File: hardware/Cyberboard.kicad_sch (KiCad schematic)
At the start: 67 parts, among them J1 Conn_01x20, J2 Conn_01x20, SW1 SW_Push, SW2 SW_Push, U1 TPS630701RNMR, U2 NX2012SA-32.768KHZ-STD-MUB-2, U3 XL-1005UBC_C22355736, U4 STM32WB55RGVx, U5 BQ24074RGT, U6 TPD2EUSB30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

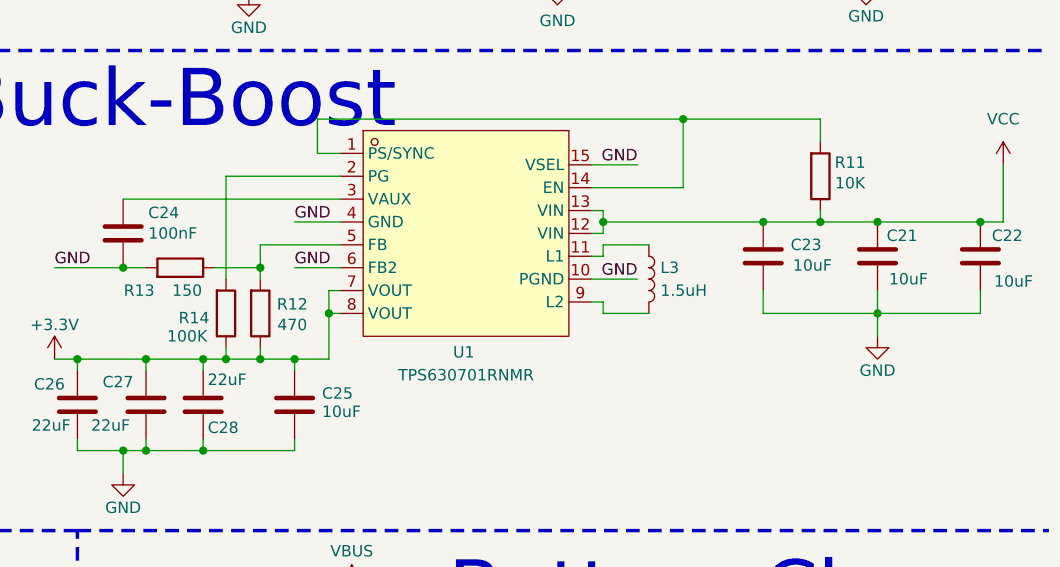
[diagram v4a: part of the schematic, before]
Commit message: forgot resistor values and change in inductor footprint
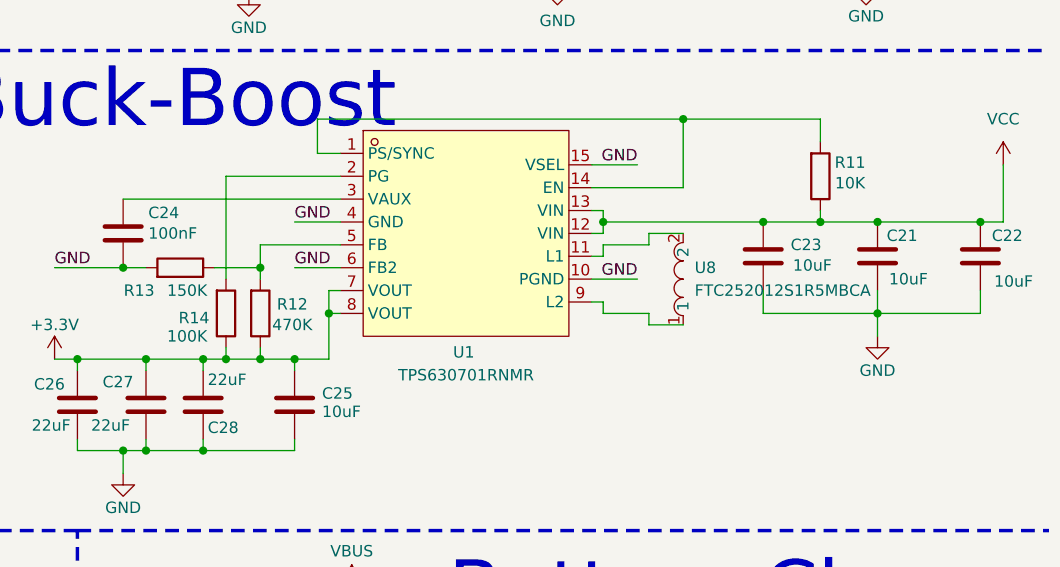
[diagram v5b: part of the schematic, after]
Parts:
- removed L3: 1.5uH, Inductor_SMD:L_0603_1608Metric, symbol Device:L
- added U8: FTC252012S1R5MBCA, lcsc:IND-SMD_L2.5-W2.0_MEKK2520TR47M, symbol lcsc:FTC252012S1R5MBCA
- R12: value 470 -> 470K
- R13: value 150 -> 150K
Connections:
- net at U1.11 (L1): now also U8.2
- net at U1.9 (L2): now also U8.1
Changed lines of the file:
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@@
 	(wire
 		(pts
+			(xy 240.03 78.74) (xy 243.84 78.74)
+		)
+		(stroke
+			(width 0)
+			(type default)
+		)
+	)
+	(wire
+		(pts
 			(xy 86.36 55.88) (xy 100.33 55.88)
 		)
@@
 	(wire
 		(pts
+			(xy 240.03 88.9) (xy 243.84 88.9)
+		)
+		(stroke
+			(width 0)
+			(type default)
+		)
+	)
+	(wire
+		(pts
 			(xy 106.68 168.91) (xy 119.38 168.91)
 		)
@@
 	(wire
 		(pts
+			(xy 240.03 87.63) (xy 240.03 88.9)
+		)
+		(stroke
+			(width 0)
+			(type default)
+		)
+	)
+	(wire
+		(pts
 			(xy 271.78 21.59) (xy 259.08 21.59)
 		)
@@
 	(wire
 		(pts
+			(xy 240.03 80.01) (xy 240.03 78.74)
+		)
+		(stroke
+			(width 0)
+			(type default)
+		)
+	)
+	(wire
+		(pts
 			(xy 265.43 77.47) (xy 276.86 77.47)
 		)
@@
 			)
 		)
-		(property "Value" "150"
+		(property "Value" "150K"
 			(at 188.722 85.09 90)
 			(effects
@@
 			)
 		)
-		(property "Value" "470"
+		(property "Value" "470K"
 			(at 200.406 88.9 0)
 			(effects
@@
 	)
 	(symbol
-		(lib_id "Device:L")
-		(at 240.03 83.82 0)
-		(unit 1)
-		(exclude_from_sim no)
-		(in_bom yes)
-		(on_board yes)
-		(dnp no)
-		(fields_autoplaced yes)
-		(property "Reference" "L3"
-			(at 241.3 82.5499 0)
-			(effects
-				(font
-					(size 1.27 1.27)
-				)
-				(justify left)
-			)
-		)
-		(property "Value" "1.5uH"
-			(at 241.3 85.0899 0)
-			(effects
-				(font
-					(size 1.27 1.27)
-				)
-				(justify left)
-			)
-		)
-		(property "Footprint" "Inductor_SMD:L_0603_1608Metric"
-			(at 240.03 83.82 0)
-			(effects
-				(font
-					(size 1.27 1.27)
-				)
-				(hide yes)
-			)
-		)
-		(property "Datasheet" "~"
-			(at 240.03 83.82 0)
-			(effects
-				(font
-					(size 1.27 1.27)
-				)
-				(hide yes)
-			)
-		)
-		(property "Description" "Inductor"
-			(at 240.03 83.82 0)
-			(effects
-				(font
-					(size 1.27 1.27)
-				)
-				(hide yes)
-			)
-		)
-		(pin "2"
-		)
-		(pin "1"
-		)
-		(instances
-			(project ""
-				(path "/3bb22019-5160-4958-be00-a0bb623b71d1"
-					(reference "L3")
-					(unit 1)
-				)
-			)
-		)
-	)
-	(symbol
 		(lib_id "power:+3.3V")
 		(at 116.84 21.59 0)
@@
 					(unit 1)
 				)
+			)
+		)
+	)
+	(symbol
+		(lib_id "lcsc:FTC252012S1R5MBCA")
+		(at 243.84 83.82 90)
+		(unit 1)
+		(exclude_from_sim no)
+		(in_bom yes)
+		(on_board yes)
+		(dnp no)
+		(fields_autoplaced yes)
+		(property "Reference" "U8"
+			(at 245.11 82.5499 90)
+			(effects
+				(font
+					(size 1.27 1.27)
+				)
+				(justify right)
+			)
+		)
+		(property "Value" "FTC252012S1R5MBCA"
+			(at 245.11 85.0899 90)
+			(effects
+				(font
+					(size 1.27 1.27)
+				)
+				(justify right)
+			)
+		)
+		(property "Footprint" "lcsc:IND-SMD_L2.5-W2.0_MEKK2520TR47M"
+			(at 251.46 83.82 0)
+			(effects
+				(font
+					(size 1.27 1.27)
+				)
+				(hide yes)
+			)
+		)
+		(property "Datasheet" ""
+			(at 243.84 83.82 0)
+			(effects
+				(font
+					(size 1.27 1.27)
+				)
+				(hide yes)
+			)
+		)
+		(property "Description" ""
+			(at 243.84 83.82 0)
+			(effects
+				(font
+					(size 1.27 1.27)
+				)
+				(hide yes)
+			)
+		)
+		(property "LCSC Part" "C5832371"
+			(at 254 83.82 0)
+			(effects
+				(font
+					(size 1.27 1.27)
+				)
+				(hide yes)
+			)
+		)
+		(pin "1"
+		)
+		(pin "2"
+		)
+		(instances
+			(project ""
+				(path "/3bb22019-5160-4958-be00-a0bb623b71d1"
+					(reference "U8")
+					(unit 1)
+				)
